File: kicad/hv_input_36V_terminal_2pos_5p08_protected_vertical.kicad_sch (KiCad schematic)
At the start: 15 parts, among them J501 TBH-1x02-5.08mm, U501 TPS1HTC100QPWPRQ1

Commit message: Update design rules
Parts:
- C501: LCSC (none) -> C115056; Vendor SKU (none) -> C115056
- C502: LCSC (none) -> C513710; Vendor SKU (none) -> C513710
- C503: LCSC (none) -> C161234; Vendor SKU (none) -> C161234
- D501: LCSC (none) -> C211388; Vendor SKU (none) -> C211388
- J501: LCSC (none) -> C480503; Vendor SKU (none) -> C480503
- R501, R505: LCSC (none) -> C106235; Vendor SKU (none) -> C106235
- R502, R503, R504, R506, R507: LCSC (none) -> C278577; Vendor SKU (none) -> C278577
- R508: LCSC (none) -> C3016445; Vendor SKU (none) -> C3016445
- R509: LCSC (none) -> C482112; Vendor SKU (none) -> C482112
- U501: LCSC (none) -> C41558366; Vendor SKU (none) -> C41558366
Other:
- company: (none) -> Janelia Research Campus
- title: Orb Weaver Design Block Mining -> mouse-joystick-pcb

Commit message: Finish v1.0 schematic
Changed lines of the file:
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@@
 		)
 		(property "Value" "PWR_FLAG"
-			(at 104.14 38.1 0)
+			(at 106.68 41.9099 0)
 			(show_name no)
 			(do_not_autoplace no)
@@
 					(size 1.27 1.27)
 				)
+				(justify left)
 			)
 		)

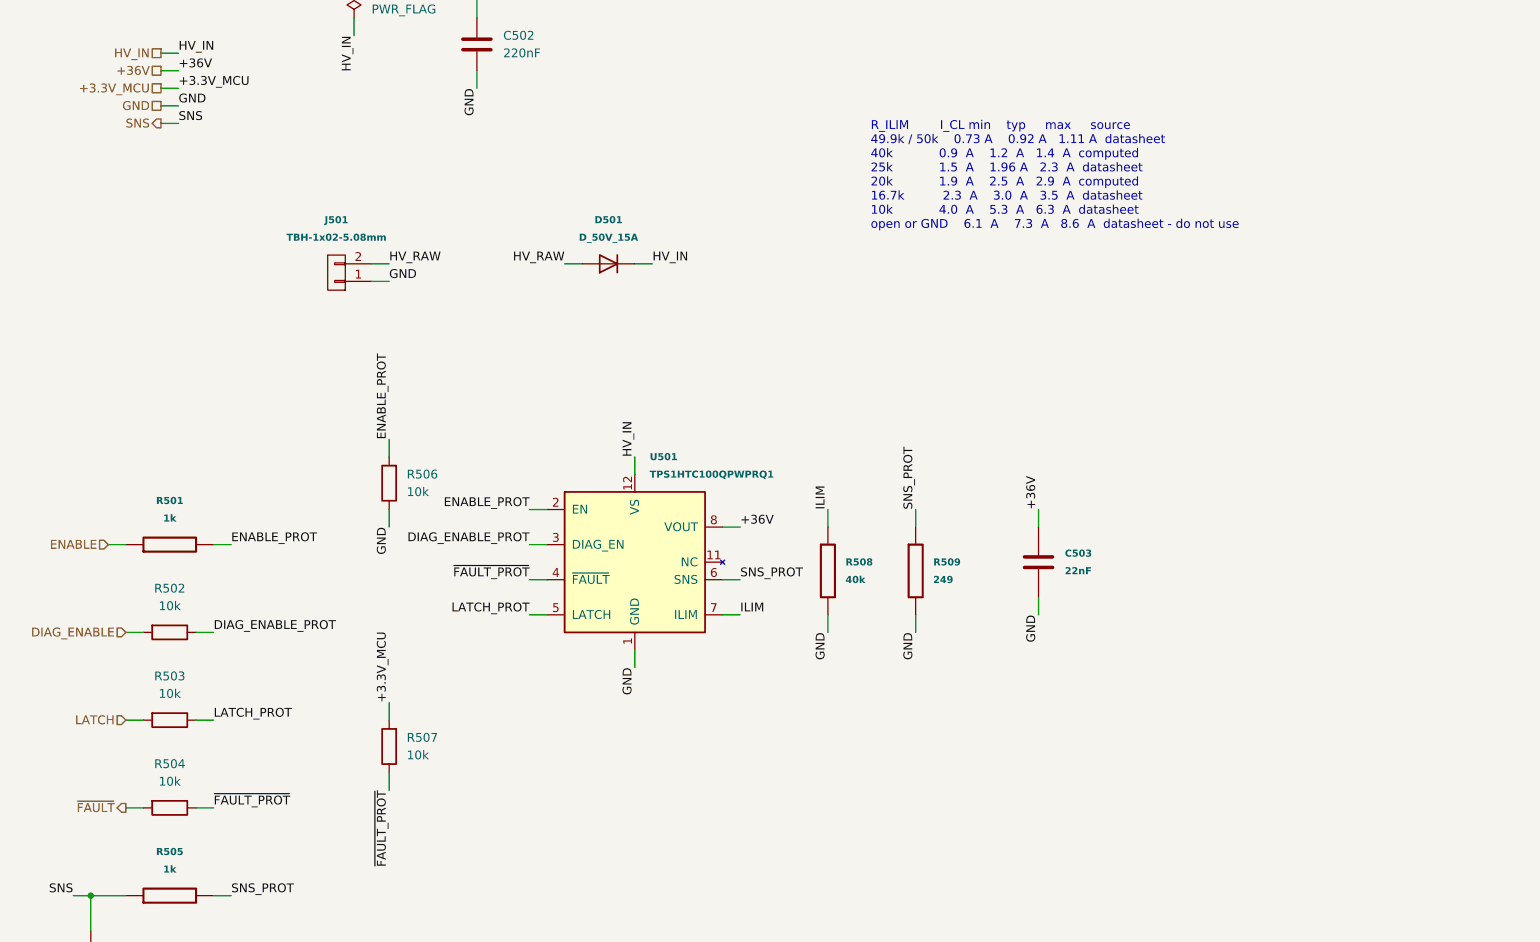
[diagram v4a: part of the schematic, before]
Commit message: Partial update of hv input block
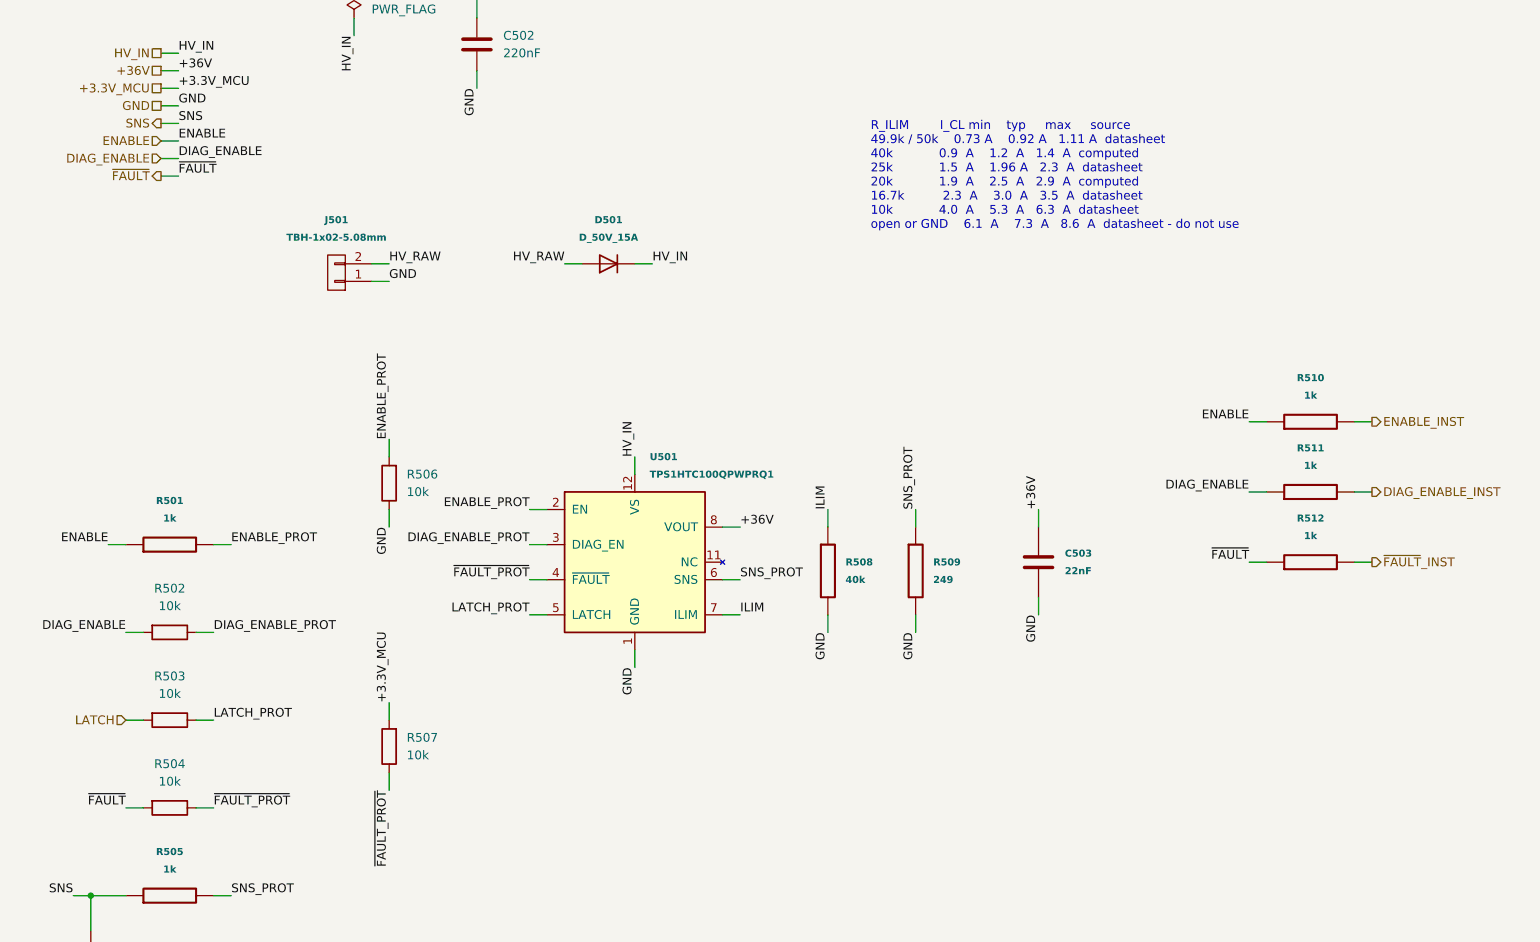
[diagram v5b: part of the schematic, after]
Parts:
- added R510, R511, R512: 1k, Resistor_SMD:R_0402_1005Metric, symbol orb_weaver_internal:All/OW-PASS-RC0402FR-071KL
- C501: LCSC C115056 -> (none); Vendor SKU C115056 -> (none)
- C502: LCSC C513710 -> (none); Vendor SKU C513710 -> (none)
- C503: LCSC C161234 -> (none); Vendor SKU C161234 -> (none)
- D501: LCSC C211388 -> (none); Vendor SKU C211388 -> (none)
- J501: LCSC C480503 -> (none); Vendor SKU C480503 -> (none)
- R501, R505: LCSC C106235 -> (none); Vendor SKU C106235 -> (none)
- R502, R503, R504, R506, R507: LCSC C278577 -> (none); Vendor SKU C278577 -> (none)
- R508: LCSC C3016445 -> (none); Vendor SKU C3016445 -> (none)
- R509: LCSC C482112 -> (none); Vendor SKU C482112 -> (none)
- U501: LCSC C41558366 -> (none); Vendor SKU C41558366 -> (none)
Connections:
- net DIAG_ENABLE: now also R511.1
- net ENABLE: now also R510.1
- net ~{FAULT}: now also R512.1
- new net DIAG_ENABLE_INST: R511.2
- new net ENABLE_INST: R510.2
- new net ~{FAULT}_INST: R512.2
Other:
- company: Janelia Research Campus -> (none)
- title: mouse-joystick-pcb -> Orb Weaver Design Block Mining

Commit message: Finish placing hv input block
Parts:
- C501: LCSC (none) -> C115056; Vendor SKU (none) -> C115056
- C502: LCSC (none) -> C513710; Vendor SKU (none) -> C513710
- C503: LCSC (none) -> C161234; Vendor SKU (none) -> C161234
- D501: LCSC (none) -> C211388; Vendor SKU (none) -> C211388
- J501: LCSC (none) -> C480503; Vendor SKU (none) -> C480503
- R501, R505, R510, R511, R512: LCSC (none) -> C106235; Vendor SKU (none) -> C106235
- R502, R503, R504, R506, R507: LCSC (none) -> C278577; Vendor SKU (none) -> C278577
- R508: LCSC (none) -> C3016445; Vendor SKU (none) -> C3016445
- R509: LCSC (none) -> C482112; Vendor SKU (none) -> C482112
- U501: LCSC (none) -> C41558366; Vendor SKU (none) -> C41558366

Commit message: Regenerate schematics
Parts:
- C501: JLC Qty 4000 -> (none); LCSC C115056 -> (none); Vendor SKU C115056 -> (none)
- C502: JLC Qty 2960 -> (none); LCSC C513710 -> (none); Placement (none) -> beside ${fc7d50ec-17b6-455e-92c7-d4ac9f6e233b:REFERENCE} VS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; Vendor SKU C513710 -> (none)
- C503: JLC Qty 211 -> (none); LCSC C161234 -> (none); Placement (none) -> beside ${fc7d50ec-17b6-455e-92c7-d4ac9f6e233b:REFERENCE} VO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; Vendor SKU C161234 -> (none)
- D501: value D_50V_15A -> SBRT15U50SP5-13; JLC Qty 253 -> (none); LCSC C211388 -> (none); Name D 50V 15A -> SBRT15U50 50 V 15 A super-barrier rectifier; Placement (none) -> beside ${fc7d50ec-17b6-455e-92c7-d4ac9f6e233b:REFERENCE} VS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; ReqValue D_50V_15A -> SBRT15U50SP5-13; Vendor SKU C211388 -> (none)
- J501: JLC Qty 248 -> (none); LCSC C480503 -> (none); Vendor SKU C480503 -> (none)
- R501, R505, R510, R511, R512: JLC Qty 10129 -> (none); LCSC C106235 -> (none); Vendor SKU C106235 -> (none)
- R502, R503, R504: JLC Qty 9560 -> (none); LCSC C278577 -> (none); Vendor SKU C278577 -> (none)
- R506: JLC Qty 9560 -> (none); LCSC C278577 -> (none); Placement (none) -> beside ${fc7d50ec-17b6-455e-92c7-d4ac9f6e233b:REFERENCE}.2 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; Vendor SKU C278577 -> (none)
- R507: JLC Qty 9560 -> (none); LCSC C278577 -> (none); Placement (none) -> beside ${fc7d50ec-17b6-455e-92c7-d4ac9f6e233b:REFERENCE}.4 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; Vendor SKU C278577 -> (none)
- R508: JLC Qty 4860 -> (none); LCSC C3016445 -> (none); Placement (none) -> beside ${fc7d50ec-17b6-455e-92c7-d4ac9f6e233b:REFERENCE}.7 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; Vendor SKU C3016445 -> (none)
- R509: JLC Qty 350 -> (none); LCSC C482112 -> (none); Placement (none) -> beside ${fc7d50ec-17b6-455e-92c7-d4ac9f6e233b:REFERENCE}.6 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; Vendor SKU C482112 -> (none)
- U501: JLC Qty 239 -> (none); LCSC C41558366 -> (none); Vendor SKU C41558366 -> (none)
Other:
- note added: "${46f86808-0f12-4b59-b5d5-64d7f6fc87f2:REFERENCE} (10 k): +36V is off until the board drives ENABLE high; supply UVLO releases at about 5.4 V. ${ccedec14-0e0a-4e56-bdc4-483a87378948:REFERENCE} (40 k) on ILIM programs the current"
- note added: "${46f86808-0f12-4b59-b5d5-64d7f6fc87f2:REFERENCE}: EN pull-down, 10 k"
- note added: "${4d9e005c-2df5-444f-86f2-c10bbc334ddf:REFERENCE} pulls the open-drain ~{FAULT} pin up to +3.3V_MCU; ${514521ed-d44b-4f06-9722-25f9009251bb:REFERENCE} brings the flag out as ~{FAULT}."
- note added: "${4d9e005c-2df5-444f-86f2-c10bbc334ddf:REFERENCE}: ~{FAULT} pull-up to +3.3V_MCU, 10 k"
- note added: "${5c7b0e5f-9255-431b-ba8e-9839802417b5:REFERENCE}: Switched-rail output capacitor; one per VOUT pins 8, 9, 10"
- note added: "${709c3d68-6a22-41fe-bb8f-1b3c74efa230:REFERENCE} bypasses HV_IN at the VS pins (12-14); ${fc7d50ec-17b6-455e-92c7-d4ac9f6e233b:REFERENCE} passes HV_IN to +36V when EN is high; ${ccedec14-0e0a-4e56-bdc4-483a87378948:REFERENCE} on ILIM (pin 7) sets the current limit; ${5c7b0e5f-9255-431b-ba8e-9839802417b5:REFERENCE} holds the switched output."
- note added: "${709c3d68-6a22-41fe-bb8f-1b3c74efa230:REFERENCE}: HV input bypass at VS; ${6584037a-df5c-481c-be6d-17e3e430d517:REFERENCE}: Reverse-polarity series diode; one per VS pins 12, 13,"
- note added: "${99bab957-2cfe-433d-b53f-598b050d3ea9:REFERENCE}, ${e120acbd-b411-4229-b638-bead54b224d1:REFERENCE} and ${80a264e6-bd6c-467a-b2b1-8c1cab27455c:REFERENCE} tap ENABLE, DIAG_ENABLE and ~{FAULT} through 1 k each for the INSTRUMENT ports; the block owns these signals, so the taps live here"
- note added: "${ccedec14-0e0a-4e56-bdc4-483a87378948:REFERENCE} = 40 kOhm on ILIM sets the current limit, giving I_CL of 0.9 A min / 1.2 A typ / 1.4 A max with a 1.5x transient peak allowance, and"
- note added: "${ccedec14-0e0a-4e56-bdc4-483a87378948:REFERENCE}: ILIM programming, 40 k"
- note added: "${ea304dcd-b413-4f8d-b22e-5f0f62389f7d:REFERENCE} feeds EN from ENABLE and ${46f86808-0f12-4b59-b5d5-64d7f6fc87f2:REFERENCE} holds it low; ${6992a98e-078f-4776-bf3b-a22e0ae0b932:REFERENCE} and ${1c88f588-9a44-4887-9bd0-3412326f1649:REFERENCE} bring DIAG_ENABLE and LATCH to their pins through 10 k each."
- note added: "${edd8ca6e-95e5-4890-b15e-f0b0125b7404:REFERENCE} brings the external 36 V supply onto HV_RAW (pin 2) and GND (pin 1); ${6584037a-df5c-481c-be6d-17e3e430d517:REFERENCE} in series passes it to HV_IN and blocks a reversed supply."
- note added: "${edd8ca6e-95e5-4890-b15e-f0b0125b7404:REFERENCE} pin 1 is GND. ${6584037a-df5c-481c-be6d-17e3e430d517:REFERENCE} (SBRT15U50SP5-13, 50 V 15 A super-barrier rectifier) blocks a reversed supply and drops under 0.44 V at these"
- note added: "${f074ca38-0248-4de7-9003-e5f54f644060:REFERENCE} = 249 Ohm at the SNS pin sets the SNS scaling (about 0.311 V per ampere); ${fcf704b4-bee3-4733-ba64-998bdbc17627:REFERENCE} (1 k) and ${37efda07-85f2-476b-ad7e-bab9b179475a:REFERENCE} (10 nF) filter it toward the SNS"
- note added: "${f074ca38-0248-4de7-9003-e5f54f644060:REFERENCE} at the SNS pin converts the sense current to a voltage; ${fcf704b4-bee3-4733-ba64-998bdbc17627:REFERENCE} and ${37efda07-85f2-476b-ad7e-bab9b179475a:REFERENCE} filter it toward the SNS port."
- note added: "${f074ca38-0248-4de7-9003-e5f54f644060:REFERENCE}: SNS sense resistor, 249 ohm"
- note added: "${fc7d50ec-17b6-455e-92c7-d4ac9f6e233b:REFERENCE} (TPS1HTC100-Q1, 6 to 60 V, 83 mohm) switches the rail. EN (pin 2) is driven from ENABLE through ${ea304dcd-b413-4f8d-b22e-5f0f62389f7d:REFERENCE} (1 k) and held low by"
- note added: "(Phoenix MSTBVA 2,5/2-G-5,08, OW-CONN-TBH-1X02-5P08-VERT, on the local orb_weaver_tht copy of the MSTBVA footprint) with a SBRT15U50SP5"
- note added: "(convention 14)."
- note added: "1 at the origin. Migrating an existing placement means changing the part and then moving the footprint by (+3.54, -10.00) so pad 1 returns to its"
- note added: "1. Entry and reverse-polarity protection"
- note added: "1.2 A limit; a fault drives about 5.2 mA, about 1.3 V). ${fcf704b4-bee3-4733-ba64-998bdbc17627:REFERENCE} (1 k) and ${37efda07-85f2-476b-ad7e-bab9b179475a:REFERENCE} (10 nF) filter it toward the SNS port (10 us); keeping ${f074ca38-0248-4de7-9003-e5f54f644060:REFERENCE} at"
- note added: "1.9 A 2.5 A 2.9 A computed 16.7k 2.3 A 3.0 A 3.5 A datasheet 10k 4.0 A 5.3 A 6.3 A datasheet open or GND 6.1 A 7.3 A 8.6 A datasheet - do not"
- note added: "14"
- note added: "2. High-side switch, input bypass, current limit and output"
- note added: "3. Enable, diagnostics and latch inputs"
- note added: "36 V entry, 2-pos 5.08 mm"
- note added: "36 V protected terminal input, vertical | series diode, TPS1HTC100 high-side switch, instrument taps"
- note added: "4. Fault output"
- note added: "4.30 mm so the terminal can move inboard, while the inboard keepout grows from 2.25 mm to 5.30 mm, so a swap in place can collide with whatever"
- note added: "5. Instrument taps"
- note added: "6. Load-current sense output"
- note added: "7. Power drive declarations"
- note added: "Analog load-current output, about 0.31 V per ampere, filtered by ${fcf704b4-bee3-4733-ba64-998bdbc17627:REFERENCE} and ${37efda07-85f2-476b-ad7e-bab9b179475a:REFERENCE} (10 us)."
- note added: "DESIGN CONTRACT"
- note added: "DESIGN NOTES"
- note added: "DIAG_ENABLE reaches DIAG_EN (pin 3) through ${6992a98e-078f-4776-bf3b-a22e0ae0b932:REFERENCE} (10 k) and must be driven high for the analog sense and the open-load and short-to-battery"
- note added: "DIAG_ENABLE series, 10 k"
- note added: "DO NOT ROTATE 180 DEGREES to make the wire entry face outboard: pin order runs the same direction in both footprints, so rotating swaps GND and"
- note added: "ENABLE series, 1 k"
- note added: "Electrically the horizontal hv_input_36V_terminal_2pos_5p08_protected block, port for port (+3.3V_MCU, +36V, DIAG_ENABLE, ENABLE, GND, HV_IN, LATCH,"
- note added: "Fault flag through ${514521ed-d44b-4f06-9722-25f9009251bb:REFERENCE} (10 k), pulled up to +3.3V_MCU by ${4d9e005c-2df5-444f-86f2-c10bbc334ddf:REFERENCE}; low during a fault."
- note added: "HV/VMOT entry rails feeding stepper drivers, brake supplies, and downstream regulation."
- note added: "INTERFACES"
- note added: "Instrument tap of DIAG_ENABLE through ${e120acbd-b411-4229-b638-bead54b224d1:REFERENCE} (1 k), INSTRUMENT class."
- note added: "Instrument tap of ENABLE through ${99bab957-2cfe-433d-b53f-598b050d3ea9:REFERENCE} (1 k), INSTRUMENT class."
- note added: "Instrument tap of ~{FAULT} through ${80a264e6-bd6c-467a-b2b1-8c1cab27455c:REFERENCE} (1 k), INSTRUMENT class."
- note added: "Instrument tap, 1 k"
- note added: "LATCH series, 10 k"
- note added: "Logic input through ${1c88f588-9a44-4887-9bd0-3412326f1649:REFERENCE} (10 k) to LATCH; selects latched shutdown or automatic retry after a fault."
- note added: "Logic input through ${6992a98e-078f-4776-bf3b-a22e0ae0b932:REFERENCE} (10 k) to DIAG_EN; must be driven high for SNS and the diagnostics, open reads low."
- note added: "Logic input through ${ea304dcd-b413-4f8d-b22e-5f0f62389f7d:REFERENCE} (1 k) to EN; ${46f86808-0f12-4b59-b5d5-64d7f6fc87f2:REFERENCE} holds EN low, so the rail is off until driven."
- note added: "Matching net labels are connected. Group order explains function; PCB placement priorities are stated below."
- note added: "No TVS and no power LED in this variant. ${709c3d68-6a22-41fe-bb8f-1b3c74efa230:REFERENCE} (220 nF, 100 V X7R) bypasses HV_IN; ${5c7b0e5f-9255-431b-ba8e-9839802417b5:REFERENCE} (22 nF, 100 V) holds the switched output. ${edd8ca6e-95e5-4890-b15e-f0b0125b7404:REFERENCE}"
- note added: "OPERATION"
- note added: "PLACE: ${edd8ca6e-95e5-4890-b15e-f0b0125b7404:REFERENCE}'s footprint has pin 1 at its origin (the horizontal part's is 10 mm off its pads), its pads are 2.08 x 3.6 mm on a 1.4 mm drill, and its courtyard reaches 5.3 mm inboard of"
- note added: "PLACE: Keep ${6584037a-df5c-481c-be6d-17e3e430d517:REFERENCE} close to ${edd8ca6e-95e5-4890-b15e-f0b0125b7404:REFERENCE} so HV_RAW stays short; the whole supply current flows through ${6584037a-df5c-481c-be6d-17e3e430d517:REFERENCE}, so give its PowerDI 5 pad copper on both sides for heat."
- note added: "PLACE: Place ${46f86808-0f12-4b59-b5d5-64d7f6fc87f2:REFERENCE} at pin 2 with a short return to GND; the series resistors can sit between the ports and the pins."
- note added: "PLACE: Place ${4d9e005c-2df5-444f-86f2-c10bbc334ddf:REFERENCE} near pin 4; ${514521ed-d44b-4f06-9722-25f9009251bb:REFERENCE} anywhere between the pin node and the port."
- note added: "PLACE: Place ${709c3d68-6a22-41fe-bb8f-1b3c74efa230:REFERENCE} at ${fc7d50ec-17b6-455e-92c7-d4ac9f6e233b:REFERENCE} pins 12-14 with a short return to pin 1 / the thermal pad."
- note added: "PLACE: Place ${ccedec14-0e0a-4e56-bdc4-483a87378948:REFERENCE} directly at pin 7 with a short return to GND; place ${5c7b0e5f-9255-431b-ba8e-9839802417b5:REFERENCE} at VOUT (pins 8-10) with a short return to GND. Tie the thermal pad (pin 15) to GND copper with vias; the"
- note added: "PLACE: Place ${f074ca38-0248-4de7-9003-e5f54f644060:REFERENCE} directly at pin 6 with a short return to GND, then ${fcf704b4-bee3-4733-ba64-998bdbc17627:REFERENCE} and ${37efda07-85f2-476b-ad7e-bab9b179475a:REFERENCE} after it; a resistor or capacitor between the pin and ${f074ca38-0248-4de7-9003-e5f54f644060:REFERENCE} changes the"
- note added: "PLACE: Place the three taps in a row near the port side of the block; their port copper is a via each (convention 1)."
- note added: "POLARITY-DEFINITE, not polarity-agnostic."
- note added: "Power driven: HV_IN"
- note added: "Protected and electronically switched 36 V high-voltage input front end on a VERTICAL, top-entry 2-position 5.08 mm pluggable terminal block"
- note added: "Protected and electronically switched 36 V high-voltage input front end on a VERTICAL, top-entry 2-position 5.08 mm pluggable terminal block — Phoenix MSTBVA 2,5/2-G-5,08, OW-CONN-TBH-1X02-5P08-VERT, on the local orb_weaver_tht copy of the MSTBVA footprint — with a SBRT15U50SP5 reverse-polarity series diode and a TPS1HTC100-Q1 smart high-side switch providing adjustable current limit, inrush/soft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"
- note added: "Protected input after ${6584037a-df5c-481c-be6d-17e3e430d517:REFERENCE} and before the switch, bypassed by ${709c3d68-6a22-41fe-bb8f-1b3c74efa230:REFERENCE}; available to the board unswitched."
- note added: "Pull-up supply for ~{FAULT} through ${4d9e005c-2df5-444f-86f2-c10bbc334ddf:REFERENCE} (10 k); draws only the pull-up current."
- note added: "ROUTE: +3.3V_MCU here is only the pull-up supply (Default class); the flag is low-current logic."
- note added: "ROUTE: All four nodes are low-current Default-class logic; nothing critical."
- note added: "ROUTE: HV_RAW is the PWR_HV_ENTRY class (0.5 mm clearance) and HV_IN PWR_HV_LOCAL; size the copper for the full supply current and keep the GND return beside the supply path from the"
- note added: "ROUTE: INSTRUMENT class to the ports; a tap that is not probed is left open at the via."
- note added: "ROUTE: SNS_PROT is a low-level analog node; route it away from the HV_IN and +36V copper and give ${37efda07-85f2-476b-ad7e-bab9b179475a:REFERENCE} a return next to ${f074ca38-0248-4de7-9003-e5f54f644060:REFERENCE}'s."
- note added: "ROUTE: Short, wide copper on both ${709c3d68-6a22-41fe-bb8f-1b3c74efa230:REFERENCE} legs; it is the local reservoir for the switch's turn-on."
- note added: "ROUTE: VS (pins 12-14) and VOUT (pins 8-10) are the PWR_HV_LOCAL current path; keep each group of pins tied together with wide copper. ILIM is a low-current Default-class node that"
- note added: "R_ILIM I_CL min typ max source 49.9k / 50k 0.73 A 0.92 A 1.11 A datasheet 40k 0.9 A 1.2 A 1.4 A computed 25k 1.5 A 1.96 A 2.3 A datasheet 20k"
- note added: "Return: terminal pin 1, switch GND (pin 1) and thermal pad (pin 15), bypass, ILIM and sense returns."
- note added: "SNS (pin 6) sources load current divided by 800 (KSNS): ${f074ca38-0248-4de7-9003-e5f54f644060:REFERENCE} (249 ohm) at the pin converts it to about 0.311 V per ampere (about 0.37 V at the"
- note added: "SNS filter series, 1 k"
- note added: "SNS output filter"
- note added: "SNS, ~FAULT), plus three 1 k instrument taps (ENABLE_INST, DIAG_ENABLE_INST, ~FAULT_INST) on the block's own signals. Signal path is terminal pin 2"
- note added: "Signal path: ${edd8ca6e-95e5-4890-b15e-f0b0125b7404:REFERENCE} pin 2 (HV_RAW) -> ${6584037a-df5c-481c-be6d-17e3e430d517:REFERENCE} anode to cathode -> HV_IN -> ${fc7d50ec-17b6-455e-92c7-d4ac9f6e233b:REFERENCE} VS (pins 12-14) -> VOUT (pins 8-10) -> +36V;"
- note added: "Smart high-side switch, analog current sense"
- note added: "Switched, current-limited 36 V rail from ${fc7d50ec-17b6-455e-92c7-d4ac9f6e233b:REFERENCE} VOUT (pins 8-10); off until ENABLE is high."
- note added: "The footprint anchor differs: the horizontal PHOENIX_1757242 is anchored 10 mm off its own pads with pin 1 at (3.54, -10.00); the vertical puts pin"
- note added: "The narrow-axis annular ring shrinks from 0.50 mm to 0.34 mm, still about 1.9x the 0.18 mm JLCPCB routine PTH minimum; the pad-to-pad gap"
- note added: "The terminal is pad-COMPATIBLE with the horizontal 5.08 mm part, not pad-IDENTICAL: pitch is 5.08 mm in both and pin order ascends in +x in both,"
- note added: "Thermal shutdown is 165 C typical, retry about 2 ms."
- note added: "These nets have an explicit ERC power source declaration."
- note added: "USB, the pyControl port, and the InstrumentPort, a reversed terminal puts the supply across those grounds instead and the diode protects nothing. The"
- note added: "aperture above it plus clearance for the plug body, its screw heads and the wire loop."
- note added: "automatic retry. ~{FAULT} (pin 4) is open-drain, pulled up by ${4d9e005c-2df5-444f-86f2-c10bbc334ddf:REFERENCE} (10 k) to +3.3V_MCU and brought out through ${514521ed-d44b-4f06-9722-25f9009251bb:REFERENCE} (10 k); low during a"
- note added: "but the pad goes from 2.5 x 2.5 mm on a 1.5 mm drill to 2.08 x 3.6 mm on a 1.4 mm drill, the Phoenix-recommended layout for the MSTBVA pin."
- note added: "currents. The terminal is polarity-definite: pin 2 is the supply, pin 1 the return. HV_IN is also a port, so a board can take the protected but"
- note added: "diagnostics; open, the internal 200 to 500 k pull-down reads it low. LATCH reaches pin 5 through ${1c88f588-9a44-4887-9bd0-3412326f1649:REFERENCE} (10 k) and selects latched shutdown or"
- note added: "fault. ENABLE, DIAG_ENABLE and ~{FAULT} each have a 1 k instrument tap (${99bab957-2cfe-433d-b53f-598b050d3ea9:REFERENCE}, ${e120acbd-b411-4229-b638-bead54b224d1:REFERENCE}, ${80a264e6-bd6c-467a-b2b1-8c1cab27455c:REFERENCE}) to the INSTRUMENT-class ports; shared bus"
- note added: "float - floating selects the internal default limit and is itself a fault state per datasheet Table 4-2. ~FAULT is open-drain, pulled up by ${4d9e005c-2df5-444f-86f2-c10bbc334ddf:REFERENCE} (10"
- note added: "improves from 2.58 mm to 3.00 mm against the 0.50 mm clearance PWR_HV_ENTRY asks of HV_IN; hole-to-hole is 3.68 mm against a 0.45 mm"
- note added: "is the vertical, top-entry Phoenix MSTBVA 2,5/2-G-5,08 (rated 12 A 250 V): the wire leaves perpendicular to the board, so the enclosure needs an"
- note added: "k) to +3.3V_MCU, which is only that pull-up supply: it and LATCH are Default-class ports, and no placing board should class +3.3V_MCU as a rail."
- note added: "limit at about 1.2 A typical (0.9 to 1.4 A) with a 1.5x transient peak allowance; ILIM must never float (an open ILIM selects the 7.3 A internal default)."
- note added: "lines are tapped by the board, these are the block's own signals (convention 14)."
- note added: "load-current sense, thermal shutdown, and an integrated inductive discharge clamp. ENABLE is pulled low through ${46f86808-0f12-4b59-b5d5-64d7f6fc87f2:REFERENCE} (10 k) so the rail stays"
- note added: "minimum. Re-run DRC after placing rather than trusting these numbers."
- note added: "must never be left open."
- note added: "off until driven. No input TVS or power-present LED is populated in this variant, unlike the 24 V barrel-jack and terminal-block variants. Intended for"
- note added: "old absolute position; the connector is the only part whose pads move. The mechanical envelope inverts: relative to pad 1 the horizontal courtyard"
- note added: "pad is the heat path at the current limit."
- note added: "pin 1, so leave that room behind it. Do not rotate it 180 degrees to turn the entry around; pin order would swap GND and the supply in board space."
- note added: "port. DIAG_EN must be driven HIGH or the analog sense and the open-load and short-to-battery diagnostics are all disabled, and ILIM must NEVER"
- note added: "reverse-polarity series diode and a TPS1HTC100-Q1 smart high-side switch providing adjustable current limit, inrush/soft-start control, analog"
- note added: "runs x -3.79 to +8.87, y -2.25 to +10.25; the vertical runs x -4.04 to +9.13, y -5.30 to +4.30. Outboard overhang collapses from 10.25 mm to"
- note added: "screw heads, and the wire loop."
- note added: "sense ratio."
- note added: "sits behind the connector even though the pitch did not change."
- note added: "terminal onward."
- note added: "the +36 V raw input in board space. The series diode blocks reverse polarity only while the input supply FLOATS; on a board whose GND is shared with"
- note added: "the pin and the filter after it preserves the ratio."
- note added: "thermal shutdown, and an integrated inductive discharge clamp."
- note added: "to HV_RAW, through ${6584037a-df5c-481c-be6d-17e3e430d517:REFERENCE} to HV_IN and the TPS1HTC100 VS pins, out VOUT as the switched +36V rail; terminal pin 1 is GND. THE TERMINAL IS"
- note added: "unswitched supply. Electrically this is the horizontal hv_input_36V_terminal_2pos_5p08_protected block plus three instrument taps."
- note added: "use"
- note added: "vertical"
- note added: "wire leaves perpendicular to the board, so the enclosure needs an aperture above the terminal plus clearance for the mating MSTB plug body, its"
- note added: "~{FAULT} output series, 10 k"
- note removed: "R_ILIM I_CL min typ max source 49.9k / 50k 0.73 A 0.92 A 1.11 A datasheet 40k 0.9 A 1.2 A 1.4 A computed 25k 1.5 A 1.96 A 2.3 A datasheet 20k 1.9 A 2.5 A 2.9 A computed 16.7k 2.3 A 3.0 A 3.5 A datasheet 10k 4.0 A 5.3 A 6.3 A datasheet open or GND 6.1 A 7.3 A 8.6 A datasheet - do not use"
- company: (none) -> Orb Weaver
- title: Orb Weaver Design Block Mining -> 36 V protected terminal input, switched, vertical
- moved on the sheet: C501, C502, C503, D501, J501, R501, R502, R503, R504, R505, R506, R507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
